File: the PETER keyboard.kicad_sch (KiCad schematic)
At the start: 142 parts, among them SW1 RotaryEncoder_Switch, SW12 RotaryEncoder_Switch

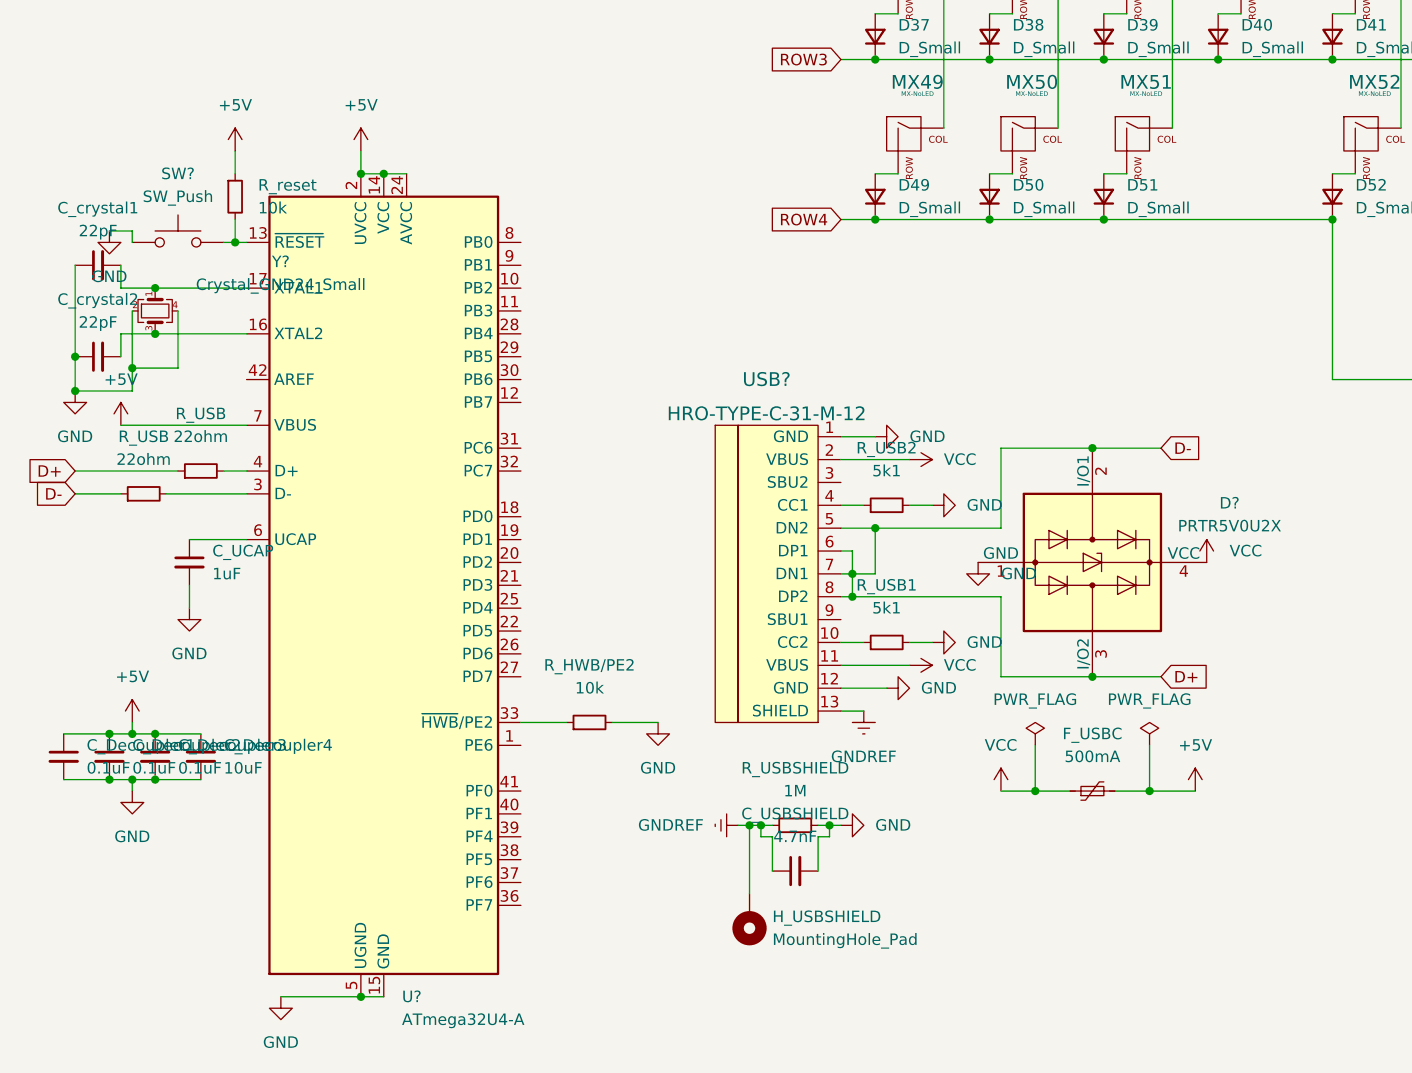
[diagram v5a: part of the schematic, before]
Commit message: footprints assigned to schematics
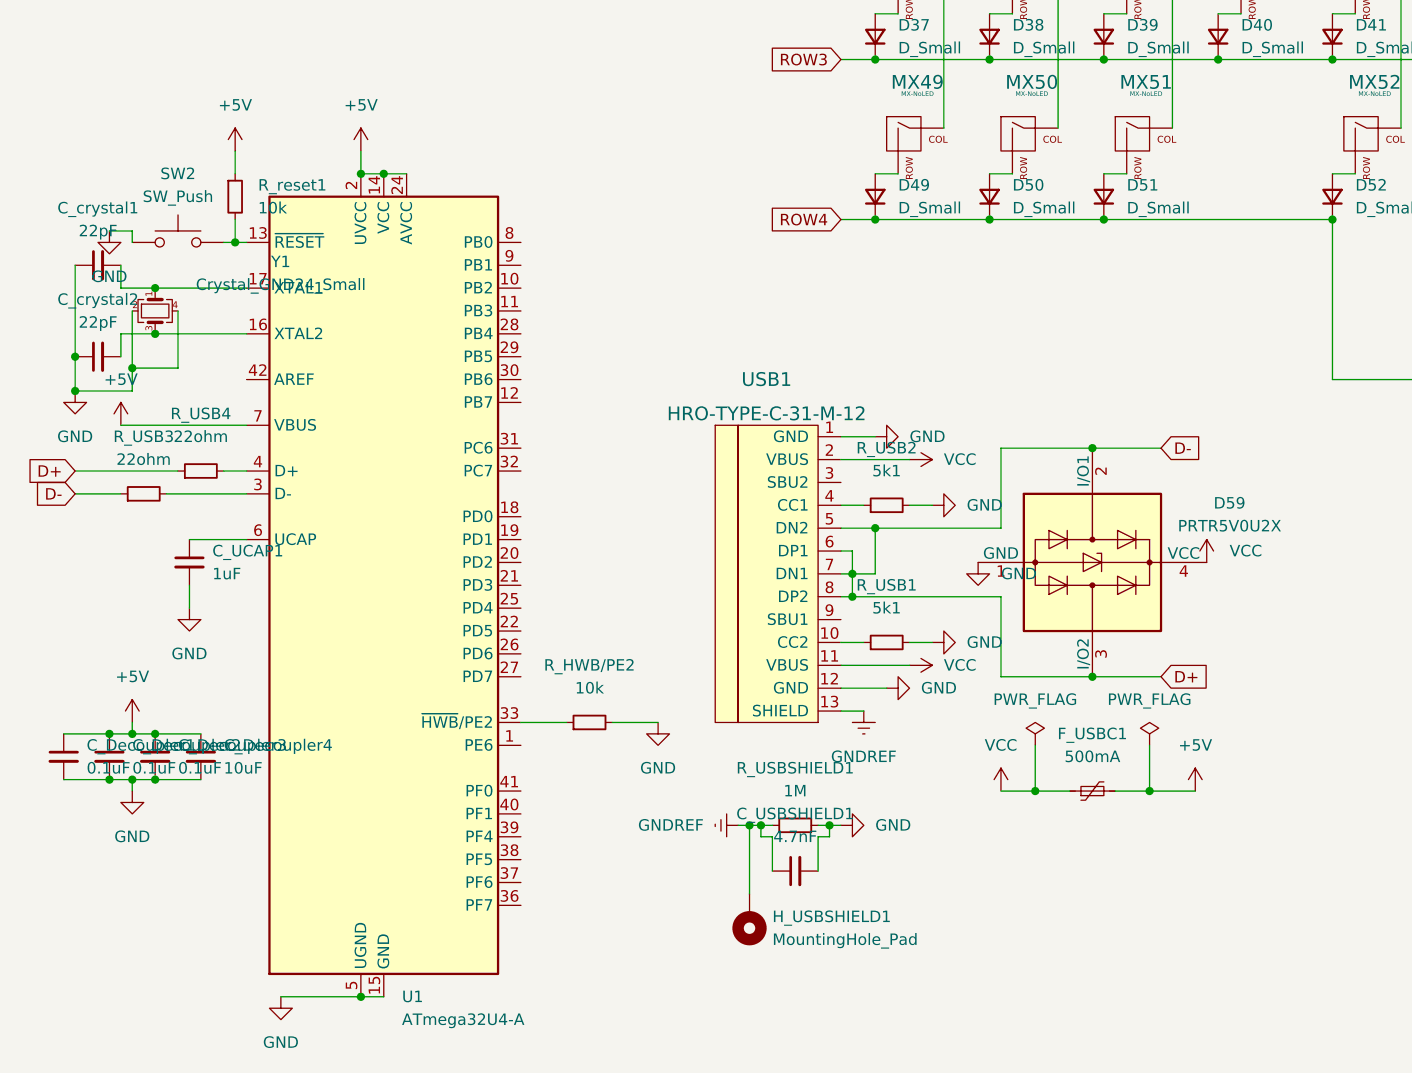
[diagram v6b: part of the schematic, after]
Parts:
- C_Decoupler1, C_Decoupler2, C_Decoupler3, C_Decoupler4, C_crystal1, C_crystal2: footprint (none) -> Capacitor_SMD:C_0805_2012Metric
- C_UCAP1: renamed from C_UCAP; footprint (none) -> Capacitor_SMD:C_0805_2012Metric
- C_USBSHIELD1: renamed from C_USBSHIELD; footprint (none) -> Capacitor_SMD:C_0805_2012Metric
- D1, D10, D11, D12, D13, D14, D15, D16, D17, D18, D19, D2, D20, D21, D22, D23, D24, D25, D26, D27, D28, D29, D3, D30, D31, D32, D33, D34, D35, D36, D37, D38, D39, D4, D40, D41, D42, D43, D44, D45, D46, D47, D48, D49, D5, D50, D51, D52, D53, D54, D55, D56, D57, D58, D6, D7, D8, D9, D_SW1, D_SW12: footprint (none) -> Diode_SMD:D_SOD-123
- F_USBC1: renamed from F_USBC; footprint (none) -> Fuse:Fuse_1206_3216Metric
- H_USBSHIELD1: renamed from H_USBSHIELD; footprint (none) -> Keebio-Parts:MountingHole
- MX1, MX10, MX11, MX12, MX13, MX14, MX15, MX16, MX17, MX18, MX19, MX2, MX20, MX21, MX22, MX23, MX26, MX27, MX28, MX29, MX3, MX30, MX31, MX32, MX33, MX34, MX35, MX38, MX39, MX4, MX40, MX41, MX42, MX43, MX44, MX45, MX46, MX47, MX48, MX5, MX50, MX55, MX56, MX57, MX58, MX6, MX7, MX8, MX9: footprint (none) -> MX_Only:MXOnly-1U-NoLED
- MX24, MX37: footprint (none) -> MX_Only:MXOnly-1.5U-NoLED
- MX25, MX36, MX49, MX51: footprint (none) -> MX_Only:MXOnly-1.25U-NoLED
- MX52: footprint (none) -> MX_Only:MXOnly-2.75U-NoLED
- MX53: footprint (none) -> MX_Only:MXOnly-6U-Centered-NoLED
- MX54: footprint (none) -> MX_Only:MXOnly-2.25U-NoLED
- R_HWB/PE2, R_USB1, R_USB2: footprint (none) -> Resistor_SMD:R_0805_2012Metric
- R_USB3, R_USB4: renamed from R_USB; footprint (none) -> Resistor_SMD:R_0805_2012Metric
- R_USBSHIELD1: renamed from R_USBSHIELD; footprint (none) -> Resistor_SMD:R_0805_2012Metric
- R_reset1: renamed from R_reset; footprint (none) -> Resistor_SMD:R_0805_2012Metric
- SW1, SW12: footprint (none) -> Keebio-Parts:RotaryEncoder_Alps_EC11E-Switch_Vertical_H20mm
- SW2: renamed from SW?; footprint (none) -> random-keyboard-parts:SKQG-1155865
- USB1: renamed from USB?; footprint (none) -> Keebio-Parts:HRO-TYPE-C-31-M-12-Assembly
- Y1: renamed from Y?; footprint (none) -> Crystal:Crystal_SMD_3225-4Pin_3.2x2.5mm
- gave numbers to parts that had none: 2

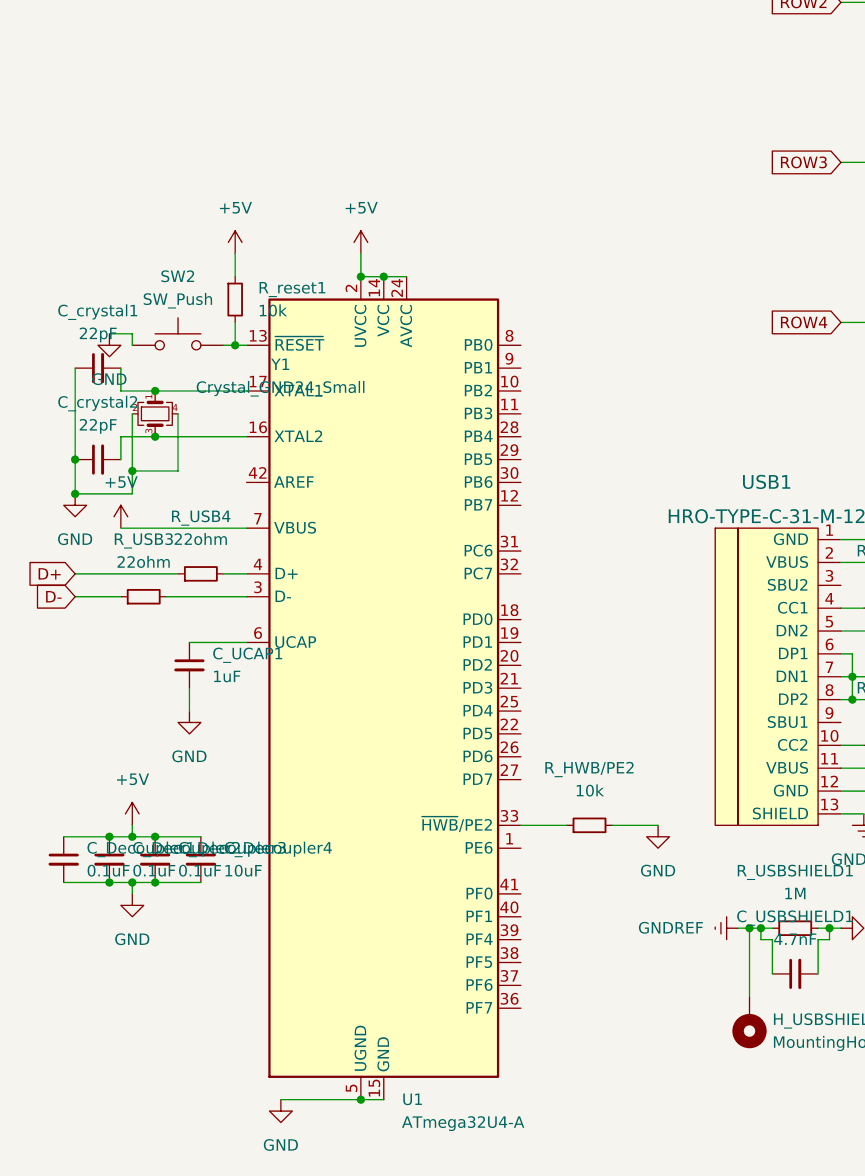
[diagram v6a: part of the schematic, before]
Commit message: reworked DSM placement, exchanged MCU for smaller
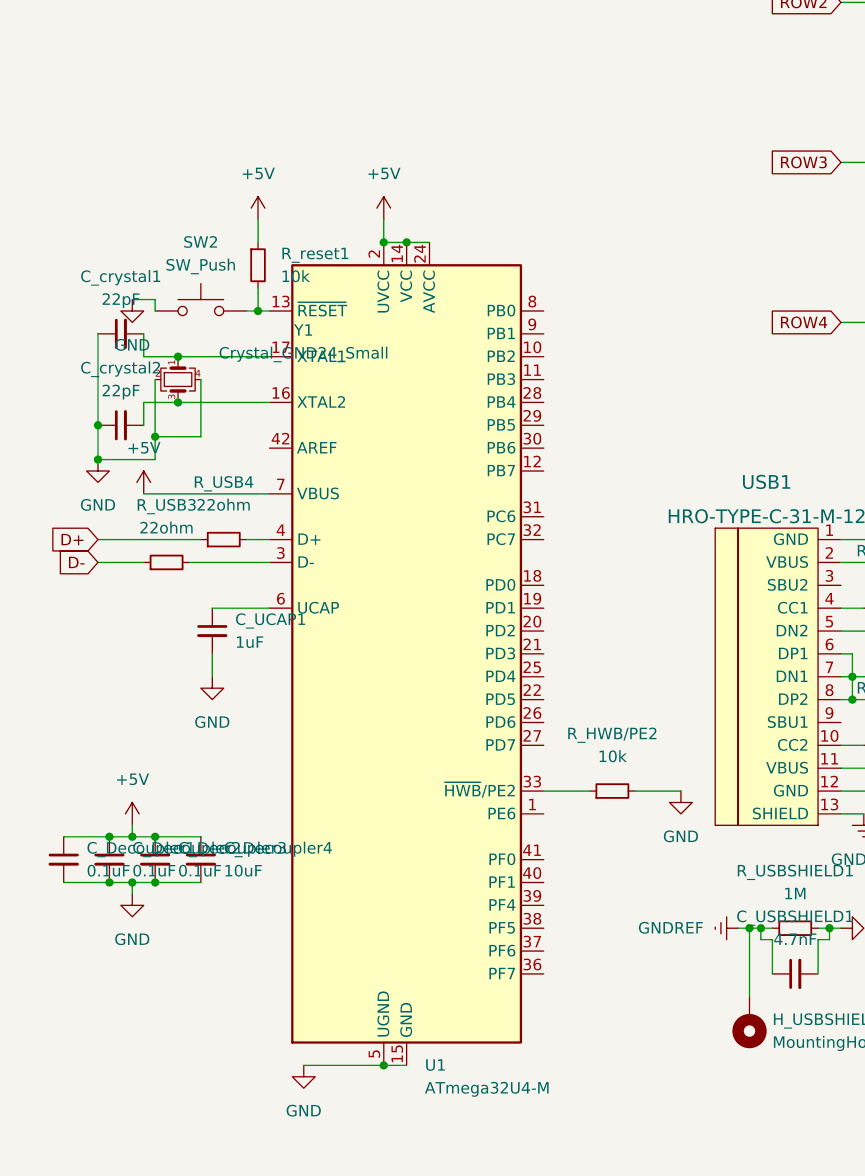
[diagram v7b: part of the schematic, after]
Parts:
- removed U1: ATmega32U4-A, Package_QFP:TQFP-44_10x10mm_P0.8mm, symbol MCU_Microchip_ATmega:ATmega32U4-A
- added U1: ATmega32U4-M, Package_DFN_QFN:QFN-44-1EP_7x7mm_P0.5mm_EP5.2x5.2mm, symbol MCU_Microchip_ATmega:ATmega32U4-M
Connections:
- net +5V: now also U1.14 (VCC), U1.2 (UVCC), U1.24 (AVCC), U1.34 (VCC), U1.44 (AVCC), U1.7 (VBUS)
- net GND: now also U1.15 (GND), U1.23 (GND), U1.35 (GND), U1.43 (GND), U1.45 (GND), U1.5 (UGND)
- net at C_crystal1.2, Y1.1: now also U1.17 (XTAL1)
- net at R_HWB/PE2.1: now also U1.33 (~{HWB}/PE2)
- net at R_reset1.2, SW2.2: now also U1.13 (~{RESET})
- net at C_UCAP1.1: now also U1.6 (UCAP)
- net at R_USB4.2: now also U1.4 (D+)
- net at R_USB3.2: now also U1.3 (D-)
- net at C_crystal2.2, Y1.3: now also U1.16 (XTAL2)
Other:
- moved on the sheet: C_UCAP1, C_crystal1, C_crystal2, R_HWB/PE2, R_USB3, R_USB4, R_reset1, SW2, Y1

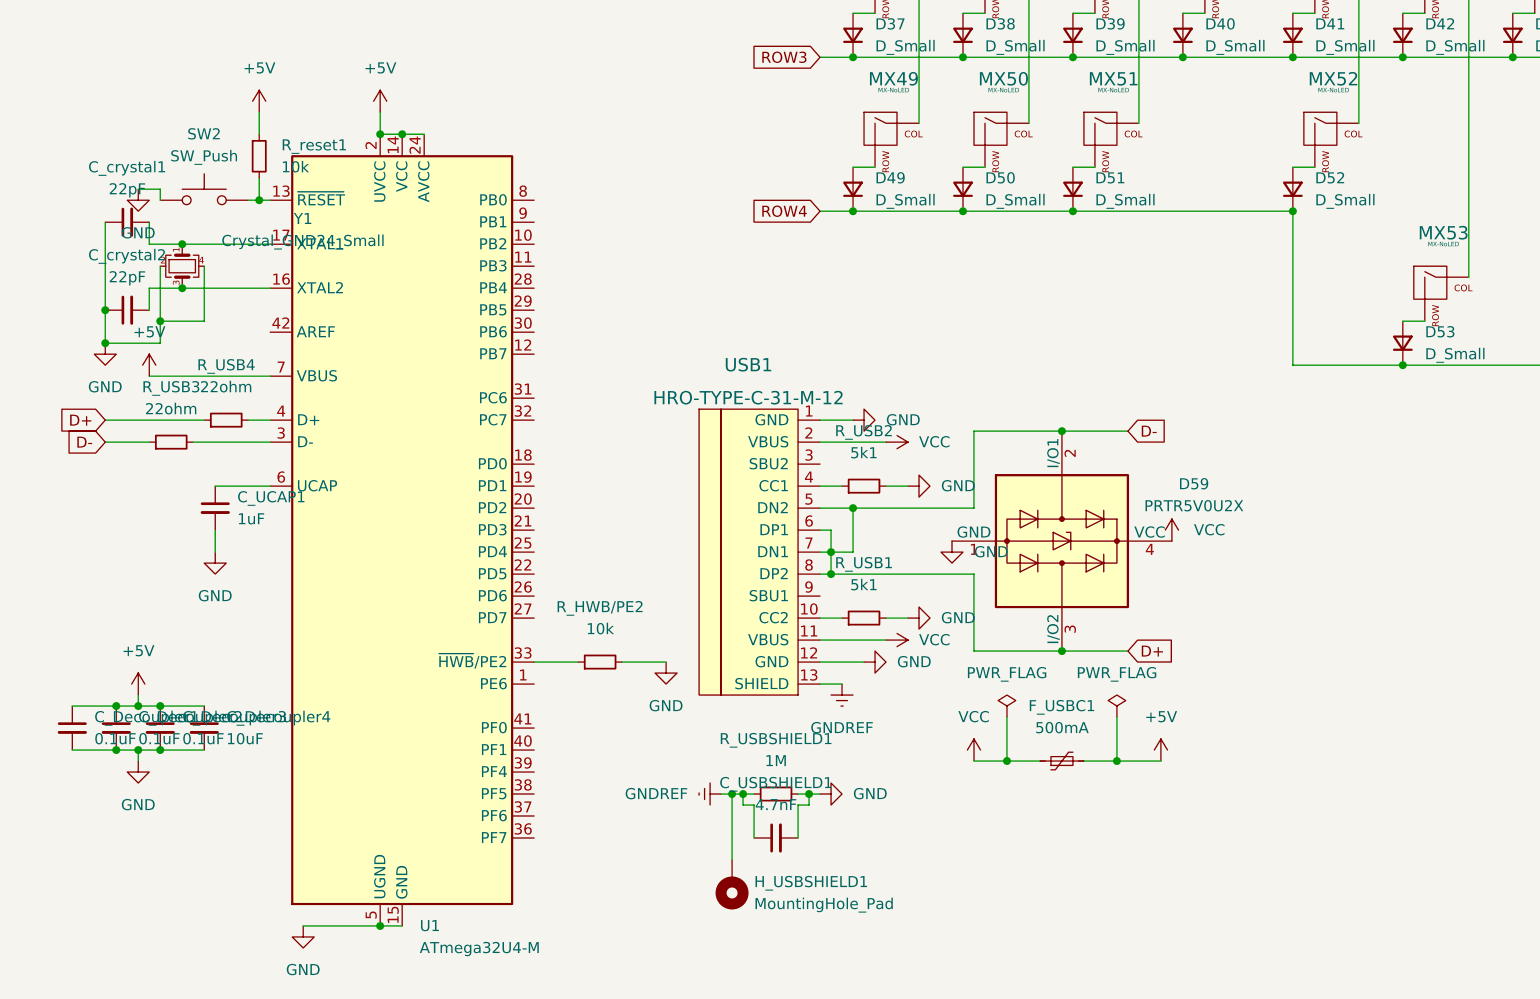
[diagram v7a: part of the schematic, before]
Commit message: trying to trace mcu, usb
no success yet
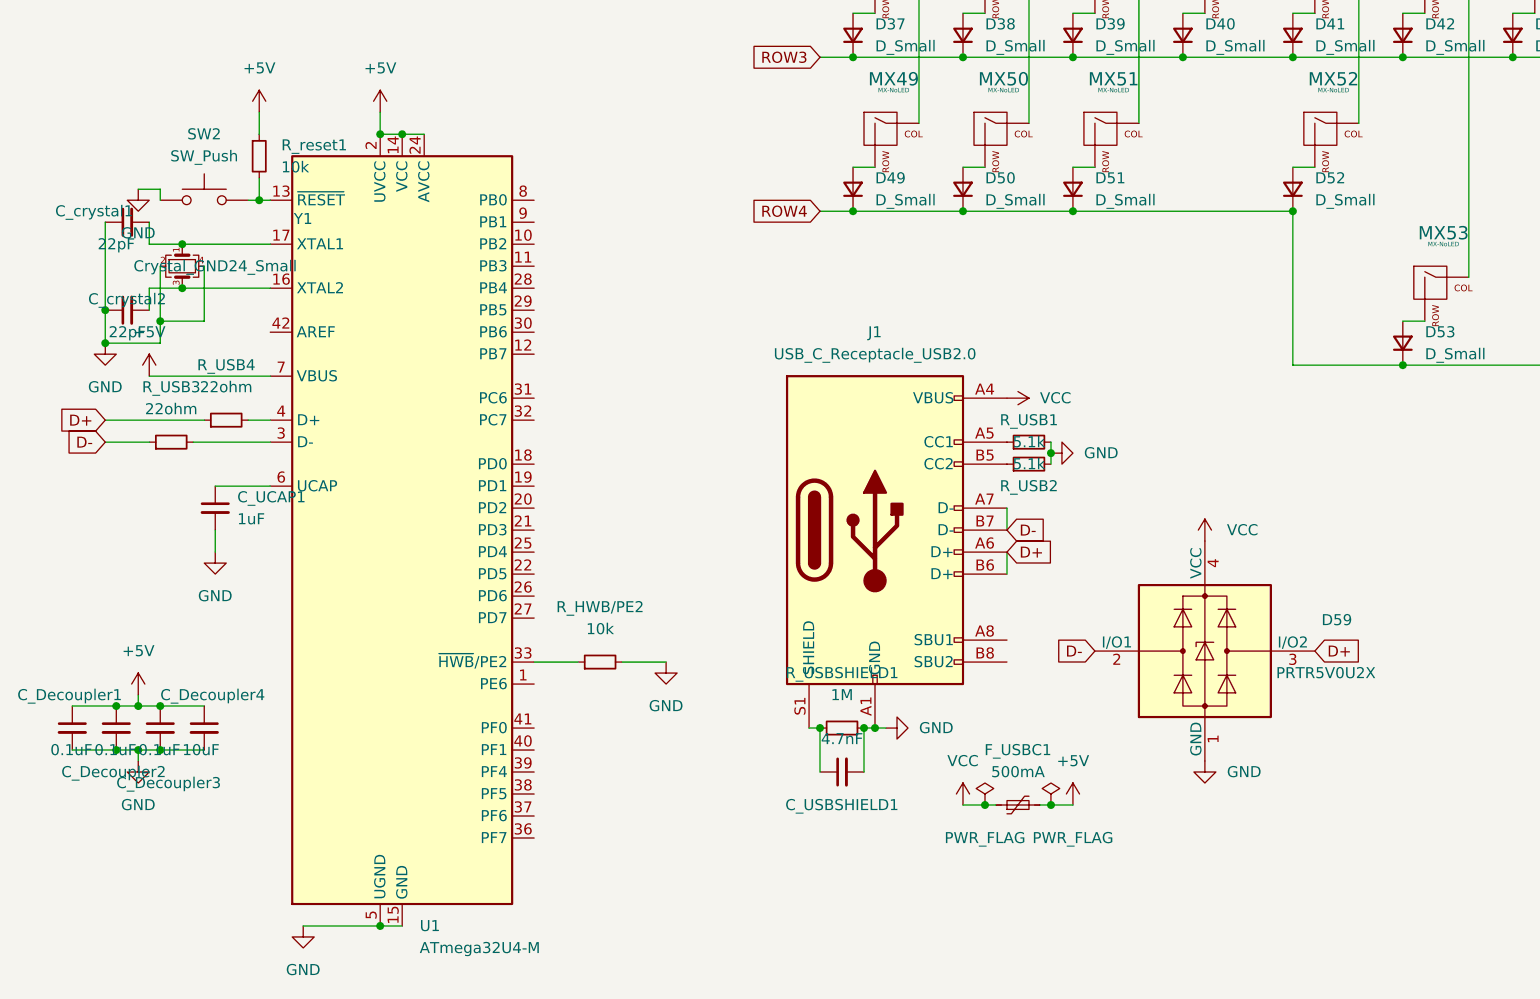
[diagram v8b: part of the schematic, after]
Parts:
- removed H_USBSHIELD1: MountingHole_Pad, Keebio-Parts:MountingHole, symbol Mechanical:MountingHole_Pad
- removed USB1: HRO-TYPE-C-31-M-12, Keebio-Parts:HRO-TYPE-C-31-M-12-Assembly, symbol keebio:HRO-TYPE-C-31-M-12
- added J1: USB_C_Receptacle_USB2.0, Connector_USB:USB_C_Receptacle_HRO_TYPE-C-31-M-12, symbol Connector:USB_C_Receptacle_USB2.0
- R_USB1, R_USB2: value 5k1 -> 5.1k
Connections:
- net D+: now also J1.A6 (D+), J1.B6 (D+); no longer D59.2 (I/O1), R_USB3.1
- net GND: now also J1.A1 (GND), J1.A12 (GND), J1.B1 (GND), J1.B12 (GND)
- net VCC: now also J1.A4 (VBUS), J1.A9 (VBUS), J1.B4 (VBUS), J1.B9 (VBUS)
- net at R_USB1.1: now also J1.A5 (CC1)
- net at R_USB2.1: now also J1.B5 (CC2)
- net GNDREF: no longer names the net of C_USBSHIELD1.1, R_USBSHIELD1.1
- net GNDREF: now also J1.S1 (SHIELD)
- new net D-: D59.2 (I/O1), J1.A7 (D-), J1.B7 (D-), R_USB3.1
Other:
- moved on the sheet: C_USBSHIELD1, D59, F_USBC1, R_USBSHIELD1
